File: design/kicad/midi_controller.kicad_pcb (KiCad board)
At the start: 2 copper layers, 166 x 166 mm, 19 parts, among them SW1 MIDI_Switch_Pushbutton_PV0H24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, SW2 MIDI_Switch_Pushbutton_PV0H24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, SW3 MIDI_Switch_Pushbutton_PV0H24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, SW4 MIDI_Switch_Pushbutton_PV0H24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, SW5 MIDI_Switch_Pushbutton_PV0H24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, SW6 MIDI_Switch_Pushbutton_PV0H24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, U1 CD74HC4067M

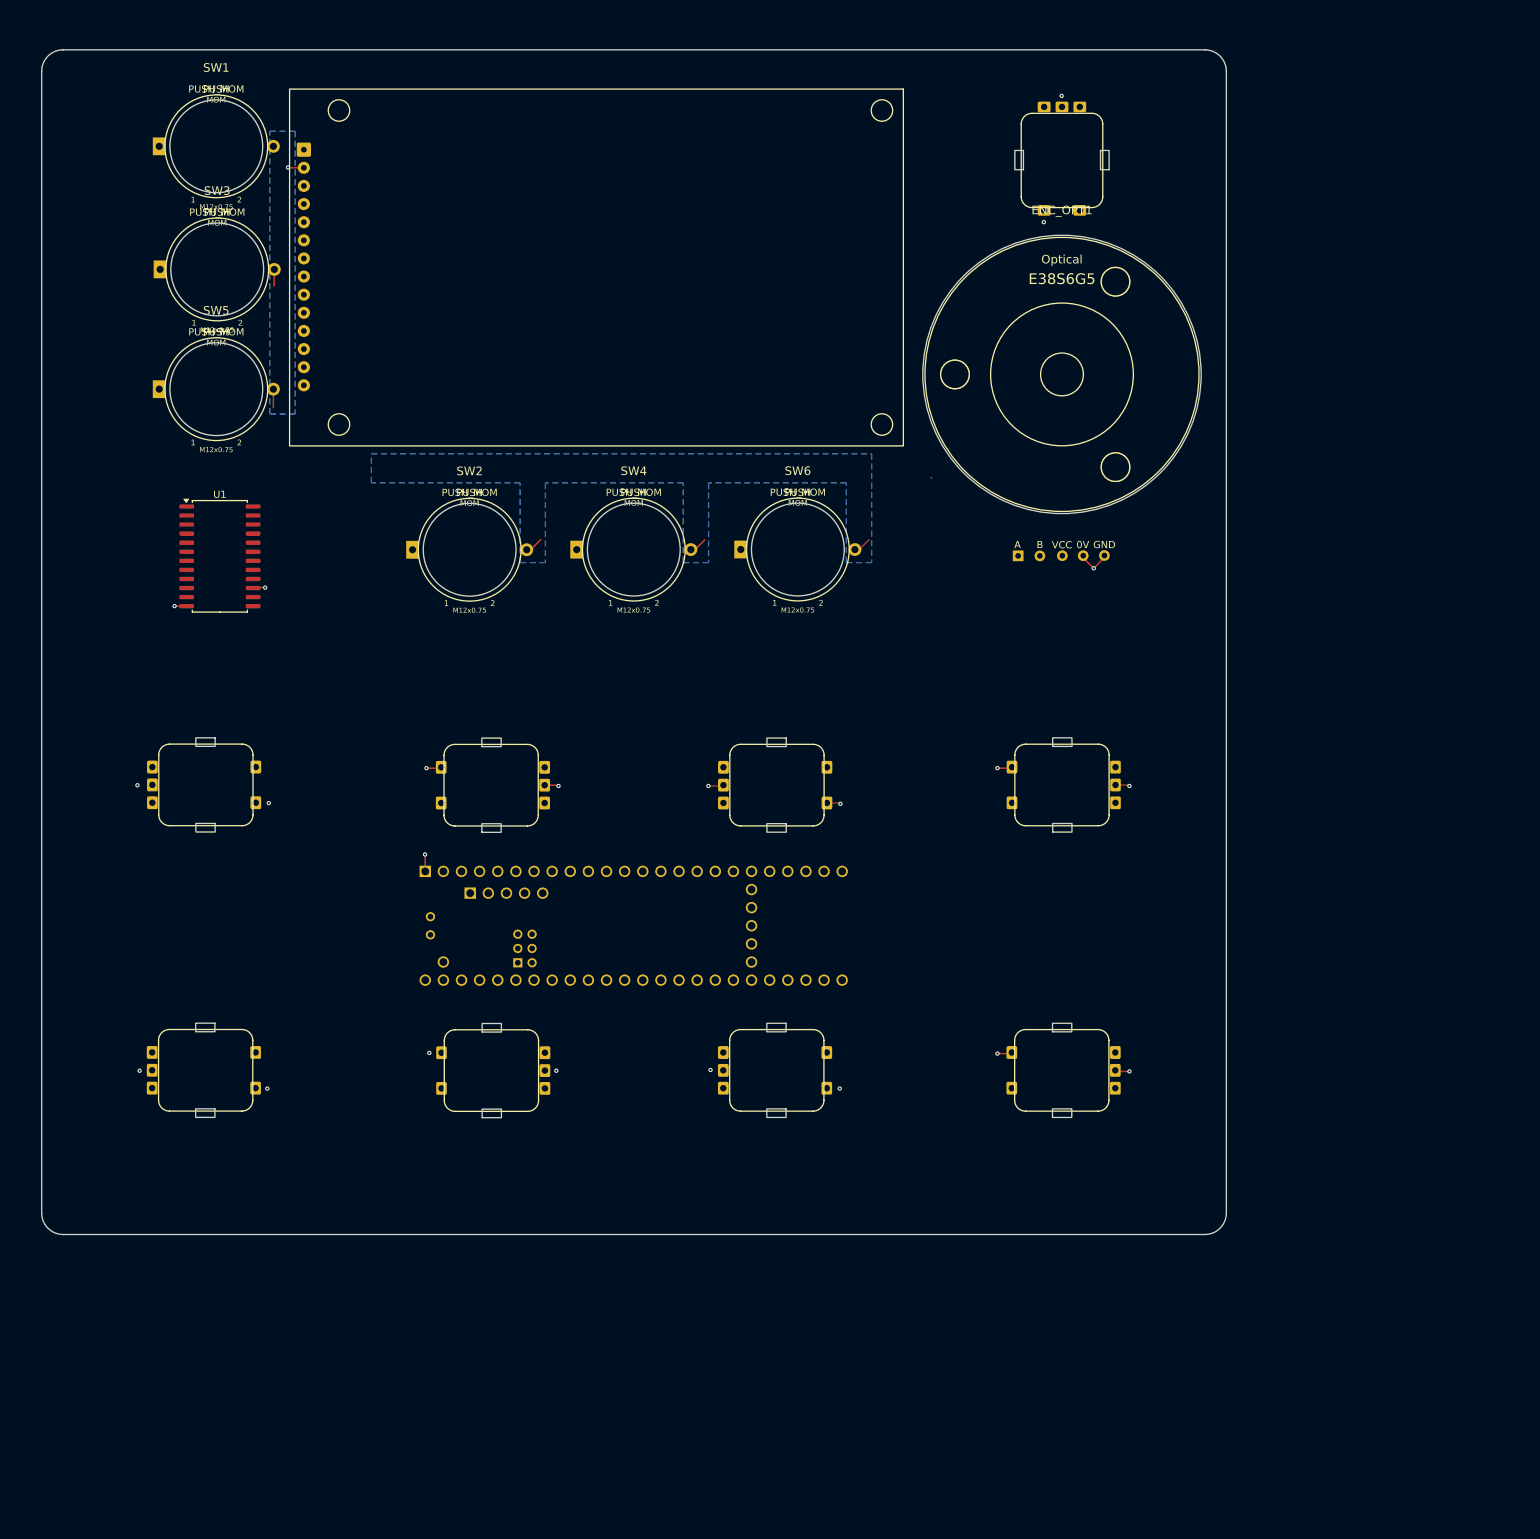
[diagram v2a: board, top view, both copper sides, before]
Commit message: Update kicad binary files
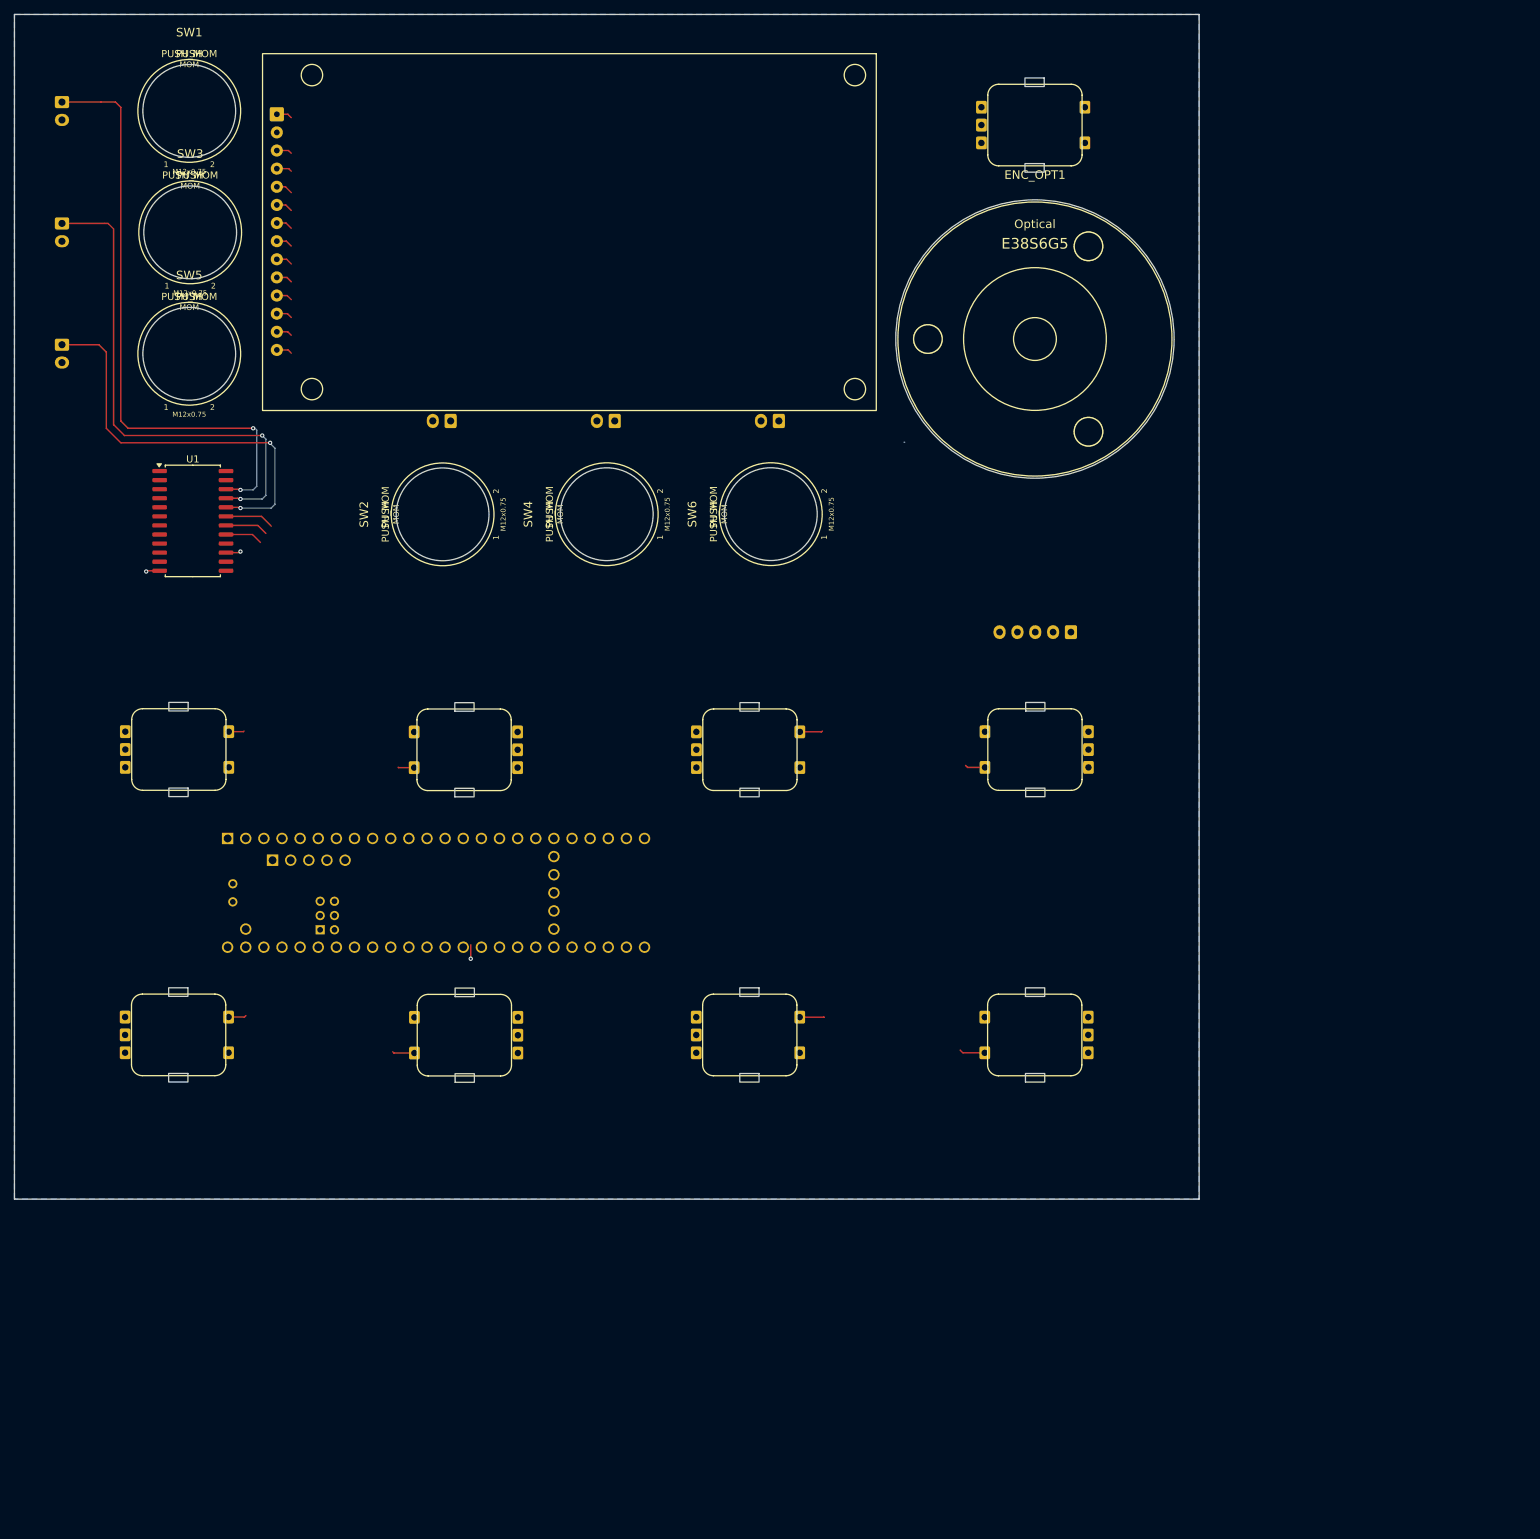
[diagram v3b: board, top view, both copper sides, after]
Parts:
- added J1: Conn_01x02_Socket, Connector_JST:JST_XH_B2B-XH-A_1x02_P2.50mm_Vertical, B.Cu at (37.9, 43.7)
- added J2: Conn_01x02_Socket, Connector_JST:JST_XH_B2B-XH-A_1x02_P2.50mm_Vertical, B.Cu at (37.9, 60.7)
- added J3: Conn_01x02_Socket, Connector_JST:JST_XH_B2B-XH-A_1x02_P2.50mm_Vertical, B.Cu at (37.9, 77.7)
- added J4: Conn_01x02_Socket, Connector_JST:JST_XH_B2B-XH-A_1x02_P2.50mm_Vertical, B.Cu at (138.4, 88.4)
- added J5: Conn_01x02_Socket, Connector_JST:JST_XH_B2B-XH-A_1x02_P2.50mm_Vertical, B.Cu at (115.4, 88.4)
- added J6: Conn_01x02_Socket, Connector_JST:JST_XH_B2B-XH-A_1x02_P2.50mm_Vertical, B.Cu at (92.4, 88.4)
- added J7: Conn_01x05, Connector_JST:JST_XH_B5B-XH-A_1x05_P2.50mm_Vertical, B.Cu at (179.3, 117.9)
- moved MCU1 28.1 mm to (90.3, 154.5)
- moved SW3 6.43 mm to (55.9, 61.9)
- moved ENC_MECH3 6.24 mm to (134.3, 134.4)
- moved ENC_MECH4 6.24 mm to (174.3, 134.4)
- moved ENC_MECH8 6.24 mm to (174.2, 174.4)
- moved ENC_MECH9 6.24 mm to (174.3, 46.9), turned to -90 degrees
- moved ENC_MECH1 6.24 mm to (54.3, 134.4)
- moved ENC_OPT1 6.24 mm to (174.3, 76.9)
- moved ENC_MECH5 6.24 mm to (54.3, 174.4)
- moved SW5 6.24 mm to (55.8, 78.9)
- moved ENC_MECH6 6.24 mm to (94.3, 174.4)
- moved ENC_MECH7 6.24 mm to (134.3, 174.4)
- moved SW2 6.24 mm to (91.3, 101.4), turned to 90 degrees
- moved SW6 6.24 mm to (137.2, 101.4), turned to 90 degrees
- moved SW1 6.24 mm to (55.8, 44.9)
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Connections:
- net /MIDI_Encoder_Matrix_2x4_with_push_buttons/1x1.QUAD_B renamed /MIDI_Encoder_Matrix_2x4_with_push_buttons/1x1.QUAD_A
- net /MIDI_Encoder_Matrix_2x4_with_push_buttons/1x2.QUAD_B renamed /MIDI_Encoder_Matrix_2x4_with_push_buttons/1x2.QUAD_A
- net /MIDI_Encoder_Matrix_2x4_with_push_buttons/1x3.QUAD_B renamed /MIDI_Encoder_Matrix_2x4_with_push_buttons/1x3.QUAD_A
- net /MIDI_Encoder_Matrix_2x4_with_push_buttons/1x4.QUAD_B renamed /MIDI_Encoder_Matrix_2x4_with_push_buttons/1x4.QUAD_A
- net /MIDI_Encoder_Matrix_2x4_with_push_buttons/2x1.QUAD_B renamed /MIDI_Encoder_Matrix_2x4_with_push_buttons/2x1.QUAD_A
- net /MIDI_Encoder_Matrix_2x4_with_push_buttons/2x2.QUAD_B renamed /MIDI_Encoder_Matrix_2x4_with_push_buttons/2x2.QUAD_A
- net /MIDI_Encoder_Matrix_2x4_with_push_buttons/2x3.QUAD_B renamed /MIDI_Encoder_Matrix_2x4_with_push_buttons/2x3.QUAD_A
- net /MIDI_Encoder_Matrix_2x4_with_push_buttons/2x4.QUAD_B renamed /MIDI_Encoder_Matrix_2x4_with_push_buttons/2x4.QUAD_A
- MCU1 pad 25: Net-(MCU1-33_MCLK2) -> Net-(J7-B)
- MCU1 pad 26: Net-(MCU1-34_RX8) -> Net-(J7-A)
- MCU1 pad 48: Net-(ENC_OPT1-+VCC) -> Net-(J7-VCC)
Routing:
- net /Buttons_Momentary/BUTTON_PUSH_MOM_01: track 0.00 -> 84.5 mm, vias 0 -> 2
- net /Buttons_Momentary/BUTTON_PUSH_MOM_02: track 0.00 -> 70.9 mm, vias 0 -> 2
- net /Buttons_Momentary/BUTTON_PUSH_MOM_03: track 0.00 -> 57.1 mm, vias 0 -> 2
- net /Buttons_Momentary/GND: track 42.0 -> 4.33 mm, vias 23 -> 2
- net /Buttons_Momentary/BUTTON_PUSH_MOM_04: track 0.00 -> 6.91 mm
- net /Buttons_Momentary/BUTTON_PUSH_MOM_05: track 0.00 -> 6.05 mm
- net /Buttons_Momentary/BUTTON_PUSH_MOM_06: track 0.00 -> 5.28 mm
- net Net-(D1-DC): track 0.00 -> 4.52 mm, vias 0 -> 1
- net /MIDI_Encoder_Matrix_2x4_with_push_buttons/2x4_SW_A: track 0.00 -> 3.62 mm
- net /MIDI_Encoder_Matrix_2x4_with_push_buttons/2x3_SW_A: track 0.00 -> 3.44 mm
- net /MIDI_Encoder_Matrix_2x4_with_push_buttons/1x3_SW_A: track 0.00 -> 3.20 mm
- net /MIDI_Encoder_Matrix_2x4_with_push_buttons/2x2_SW_A: track 0.00 -> 3.10 mm
- net /MIDI_Encoder_Matrix_2x4_with_push_buttons/1x4_SW_A: track 0.00 -> 2.84 mm
- net /MIDI_Encoder_Matrix_2x4_with_push_buttons/2x1_SW_A: track 0.00 -> 2.51 mm
- net Net-(D1-SDI/MOSI): track 0.00 -> 2.34 mm
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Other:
- outline, holes or cut-outs redrawn
- board text removed: "A3"

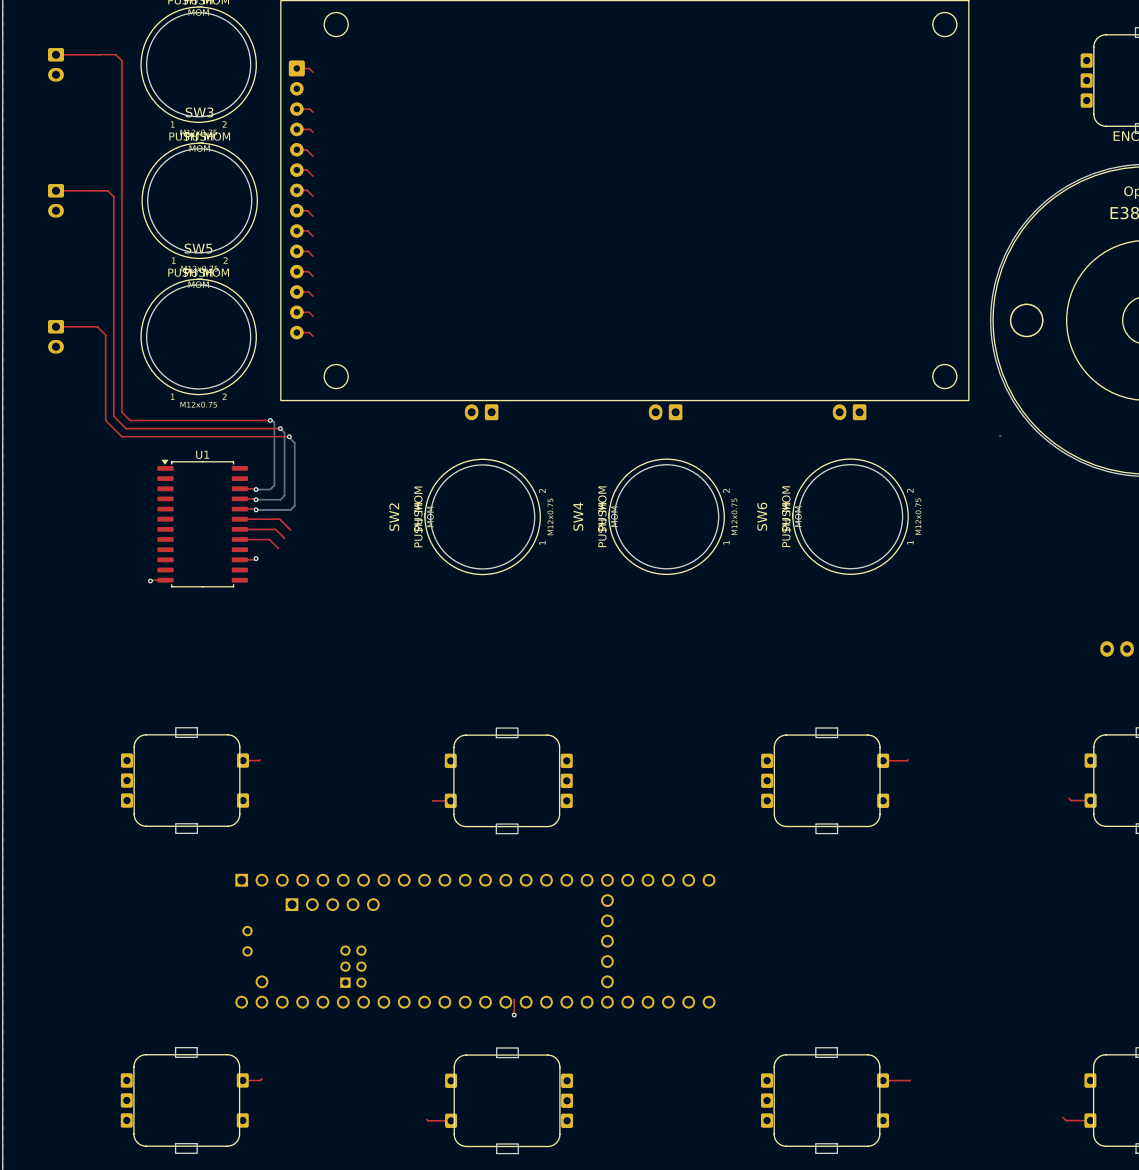
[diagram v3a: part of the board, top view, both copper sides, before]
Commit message: Update kicad binary files
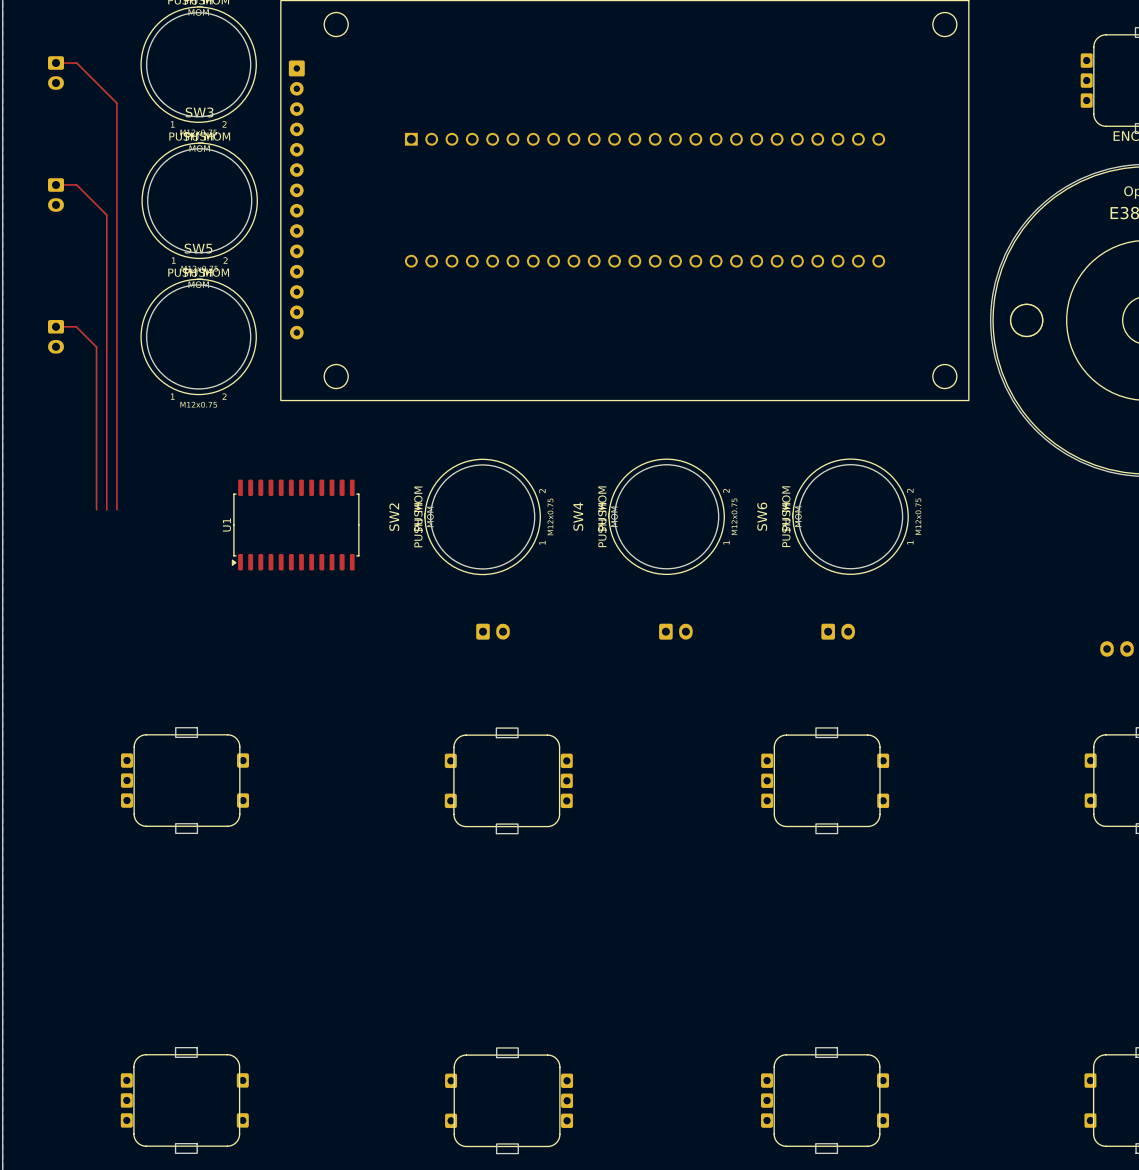
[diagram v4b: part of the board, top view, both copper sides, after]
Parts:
- moved MCU1 95.0 mm to (111.6, 61.9)
- moved J4 27.7 mm to (134.4, 115.8), turned to 0 degrees
- moved J5 27.5 mm to (114.2, 115.8), turned to 0 degrees
- moved J6 27.5 mm to (91.3, 115.8), turned to 0 degrees
- moved U1 11.7 mm to (68.0, 102.4), turned to 90 degrees
- moved J1 1.03 mm to (37.9, 44.7)
- moved J2 0.73 mm to (37.9, 59.9)
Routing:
- net /Buttons_Momentary/BUTTON_PUSH_MOM_03: track 57.1 -> 26.5 mm, vias 2 -> 0
- net /Buttons_Momentary/BUTTON_PUSH_MOM_02: track 70.9 -> 44.8 mm, vias 2 -> 0
- net /Buttons_Momentary/BUTTON_PUSH_MOM_01: track 84.5 -> 60.5 mm, vias 2 -> 0
- net /Buttons_Momentary/BUTTON_PUSH_MOM_04: track 6.91 -> 0.00 mm
- net /Buttons_Momentary/BUTTON_PUSH_MOM_05: track 6.05 -> 0.00 mm
- net /Buttons_Momentary/BUTTON_PUSH_MOM_06: track 5.28 -> 0.00 mm
- net Net-(D1-DC): track 4.52 -> 0.00 mm, vias 1 -> 0
- net /Buttons_Momentary/GND: track 4.33 -> 0.00 mm, vias 2 -> 0
- net /MIDI_Encoder_Matrix_2x4_with_push_buttons/2x4_SW_A: track 3.62 -> 0.00 mm
- net /MIDI_Encoder_Matrix_2x4_with_push_buttons/2x3_SW_A: track 3.44 -> 0.00 mm
- net /MIDI_Encoder_Matrix_2x4_with_push_buttons/1x3_SW_A: track 3.20 -> 0.00 mm
- net /MIDI_Encoder_Matrix_2x4_with_push_buttons/2x2_SW_A: track 3.10 -> 0.00 mm
- net /MIDI_Encoder_Matrix_2x4_with_push_buttons/1x4_SW_A: track 2.84 -> 0.00 mm
- net /MIDI_Encoder_Matrix_2x4_with_push_buttons/2x1_SW_A: track 2.51 -> 0.00 mm
- net Net-(D1-SDI/MOSI): track 2.34 -> 0.00 mm
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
